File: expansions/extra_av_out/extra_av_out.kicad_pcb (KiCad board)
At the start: 4 copper layers, 75.8 x 88.1 mm, 40 parts, among them J1 Conn_02x25_Odd_Even, J2 SJ1-3533NG, J3 PLT133/T10W, J4 VGA, U1 ADV7125KSTZ140, U2 PCM5142PW, U3 74HCT2G17GW

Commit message: update extra_av_out board to v1.1
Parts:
- removed C12, C14, C6: 10u, custom_components:SM0603_Capa_libcms
- added D2: PESD5V0V4UW, Package_TO_SOT_SMD:SOT-665, B.Cu at (68.4, 78.3)
- added D3: PESD12VL2BT, Package_TO_SOT_SMD:SOT-23, B.Cu at (100.6, 71.0)
- added D4: PESD5V0U4BW, Package_TO_SOT_SMD:SOT-665, B.Cu at (74.7, 70.8)
- added FB1: MPZ1608S102ATA00, custom_components:SM0603_Resistor_libcms, F.Cu at (53.3, 81.9)
- added FB2: MPZ1608S102ATA00, custom_components:SM0603_Resistor_libcms, F.Cu at (53.3, 80.2)
- added MH1: MountingHole, MountingHole:MountingHole_3.2mm_M3_ISO14580, F.Cu at (53.3, 29.0)
- added MH2: MountingHole, MountingHole:MountingHole_3.2mm_M3_ISO14580, F.Cu at (53.3, 86.5)
- added MH3: MountingHole, MountingHole:MountingHole_3.2mm_M3_ISO14580, F.Cu at (115.5, 68.3)
- added MH4: MountingHole, MountingHole:MountingHole_3.2mm_M3_ISO14580_Pad, F.Cu at (94.9, 79.9)
- added MH5: MountingHole, MountingHole:MountingHole_3.2mm_M3_ISO14580_Pad, F.Cu at (66.0, 38.4)
- added Q1: BC847, Package_TO_SOT_SMD:SOT-23, B.Cu at (61.6, 71.8)
- added R10: 47, custom_components:SM0603_Resistor_libcms, B.Cu at (70.3, 70.5)
- added R11: 47, custom_components:SM0603_Resistor_libcms, B.Cu at (72.0, 70.5)
- added R12: 10k, custom_components:SM0603_Resistor_libcms, B.Cu at (58.0, 71.9)
- added R13: 4.7k, custom_components:SM0603_Resistor_libcms, B.Cu at (58.0, 73.6)
- added R9: 47, custom_components:SM0603_Resistor_libcms, B.Cu at (68.6, 70.5)
- moved C9 8.91 mm to (91.9, 68.8), turned to 0 degrees
- moved C5 8.18 mm to (85.6, 70.5)
- moved C8 7.95 mm to (91.9, 65.5), turned to 180 degrees
- moved U2 7.56 mm to (88.7, 65.8)
- moved R1 7.56 mm to (82.1, 68.7)
- moved C3 6.70 mm to (91.9, 70.5), turned to 180 degrees
- moved C7 6.54 mm to (91.9, 67.2), turned to 180 degrees
- moved C10 5.57 mm to (85.6, 68.9), turned to 0 degrees
- moved C4 4.48 mm to (91.9, 63.8), turned to 180 degrees
- moved J2 4.24 mm to (102.6, 82.2)
- moved C13 3.00 mm to (103.5, 68.1)
- moved C21 3.00 mm to (113.5, 73.7)
- moved J3 2.76 mm to (115.0, 76.3)
- moved R2 2.18 mm to (98.8, 67.6)
- moved R3 2.18 mm to (101.0, 67.6)
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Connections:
- net Net-(C11-Pad2) renamed /AL_OUT
- net Net-(C13-Pad1) renamed /AR_OUT
- net Net-(J4-Pad1) renamed /R_OUT
- net Net-(J4-Pad2) renamed /G_OUT
- net Net-(J4-Pad3) renamed /B_OUT
- J1 pad 1: Net-(J1-Pad1) -> unconnected-(J1-Pin_1-Pad1)
- J1 pad 2: Net-(J1-Pad2) -> unconnected-(J1-Pin_2-Pad2)
- J1 pad 3: Net-(J1-Pad3) -> unconnected-(J1-Pin_3-Pad3)
- J1 pad 39: Net-(J1-Pad39) -> unconnected-(J1-Pin_39-Pad39)
- J1 pad 4: Net-(J1-Pad4) -> unconnected-(J1-Pin_4-Pad4)
- J1 pad 41: Net-(J1-Pad41) -> unconnected-(J1-Pin_41-Pad41)
- J1 pad 44: Net-(J1-Pad44) -> unconnected-(J1-Pin_44-Pad44)
- J1 pad 5: Net-(J1-Pad5) -> unconnected-(J1-Pin_5-Pad5)
- J1 pad 6: Net-(J1-Pad6) -> unconnected-(J1-Pin_6-Pad6)
- J4 pad 11: Net-(J4-Pad11) -> unconnected-(J4-ID0/RES-Pad11)
- J4 pad 12: Net-(J4-Pad12) -> unconnected-(J4-ID1/SDA-Pad12)
- J4 pad 15: Net-(J4-Pad15) -> unconnected-(J4-ID3/SCL-Pad15)
- J4 pad 4: Net-(J4-Pad4) -> /VGA_CS_75
- U2 pad 11: /SDA -> /SDA_F
- U2 pad 12: /SCL -> /SCL_F
- U2 pad 13: Net-(U2-Pad13) -> unconnected-(U2-GPIO5/ATT0-Pad13)
- U2 pad 14: Net-(U2-Pad14) -> unconnected-(U2-GPIO4/MAST-Pad14)
- U2 pad 15: Net-(U2-Pad15) -> unconnected-(U2-GPIO3/AGNS-Pad15)
- U2 pad 19: Net-(U2-Pad19) -> unconnected-(U2-GPIO6/FLT-Pad19)
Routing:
- net /SCL_F: track 0.00 -> 61.4 mm, vias 0 -> 2
- net /SCL: track 72.9 -> 13.3 mm, vias 1 -> 0
- net /SDA: track 70.4 -> 11.8 mm, vias 1 -> 0
- net /SDA_F: track 0.00 -> 56.2 mm, vias 0 -> 2
- net /I2S_WS: track 87.4 -> 55.9 mm
- net /I2S_BCK: track 80.7 -> 51.1 mm
- net /I2S_DATA: track 80.5 -> 50.9 mm
- net GND: track 76.1 -> 104.4 mm, vias 440 -> 148
- net /VGA_VS_TTL: track 17.3 -> 25.5 mm
- net Net-(Q1-E): track 0.00 -> 5.99 mm
- net /DVDD5: track 3.12 -> 9.08 mm
- net /VGA_CS_75: track 0.00 -> 4.91 mm
- net /VGA_HS: track 8.39 -> 13.0 mm, vias 0 -> 1
- net Net-(Q1-B): track 0.00 -> 4.09 mm
- net /R_OUT: track 25.2 -> 29.0 mm, vias 0 -> 1
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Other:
- board size 75.8 x 88.1 mm -> 76.3 x 88.1 mm
- net class Default removed
- board text added: "extra_av_out v1.1"
- board text removed: "extra_av_out v1.0"

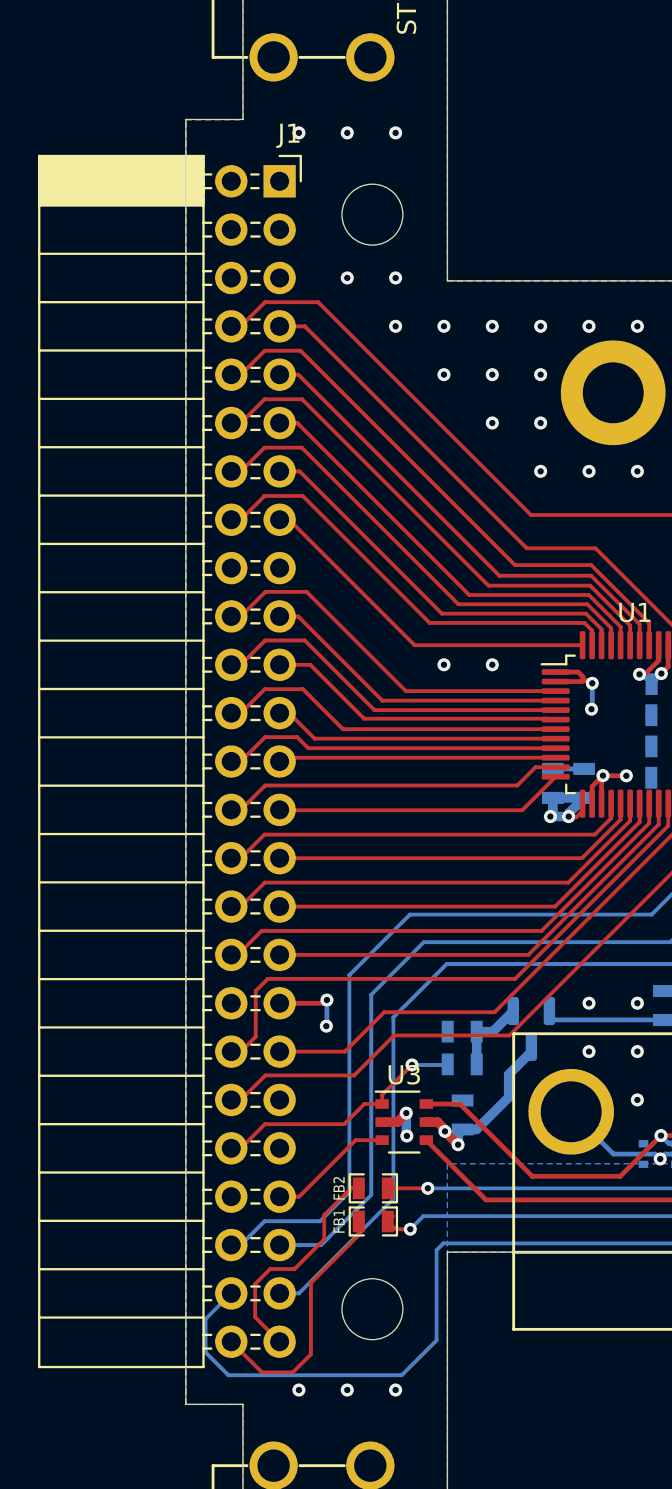
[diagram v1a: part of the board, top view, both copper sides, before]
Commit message: extra_av_out: minor adjustment on J1 position
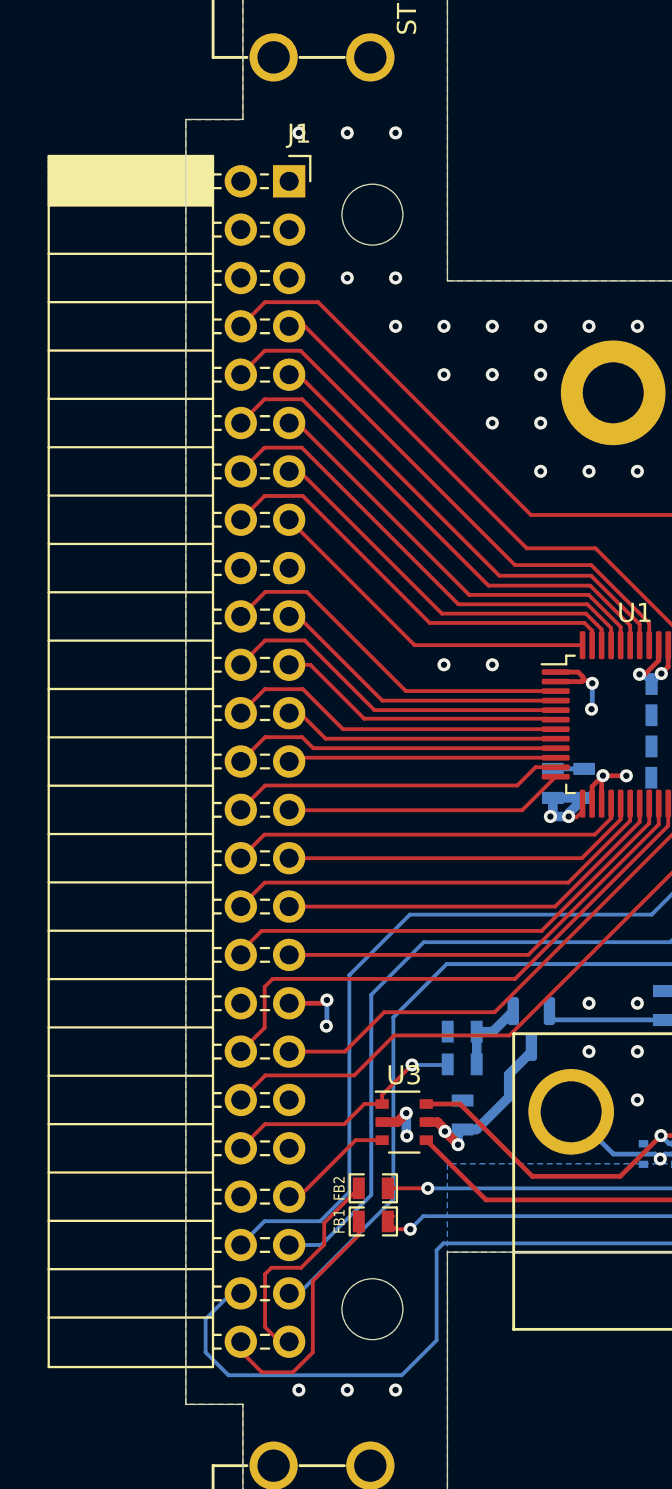
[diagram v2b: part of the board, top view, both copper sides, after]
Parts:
- moved J1 0.50 mm to (48.9, 27.2)
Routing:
- net /SDA: track 11.8 -> 11.3 mm
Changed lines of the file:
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@@
   )
   (footprint "Connector_PinSocket_2.54mm:PinSocket_2x25_P2.54mm_Horizontal" (layer "F.Cu")
-    (at 48.42579 27.24871)
+    (at 48.92579 27.24871)
     (descr "Through hole angled socket strip, 2x25, 2.54mm pitch, 8.51mm socket length, double cols (from Kicad 4.0.7), script generated")
     (tags "Through hole angled socket strip THT 2x25 2.54mm double row")
@@
   (segment (start 57.8 77.86) (end 57.8 77.302) (width 0.5) (layer "B.Cu") (net 11))
   (segment (start 58.04 77.062) (end 58.768 77.062) (width 0.5) (layer "B.Cu") (net 11))
+  (segment (start 47.49708 89.82) (end 49.12 89.82) (width 0.2) (layer "F.Cu") (net 12))
+  (segment (start 50.17 88.77) (end 50.17 85.02) (width 0.2) (layer "F.Cu") (net 12))
+  (segment (start 50.17 85.02) (end 52.586 82.604) (width 0.2) (layer "F.Cu") (net 12))
   (segment (start 52.586 82.604) (end 52.586 81.89) (width 0.2) (layer "F.Cu") (net 12))
   (segment (start 45.88579 88.20871) (end 47.49708 89.82) (width 0.2) (layer "F.Cu") (net 12))
-  (segment (start 49.12 89.82) (end 50.07 88.87) (width 0.2) (layer "F.Cu") (net 12))
-  (segment (start 50.07 88.87) (end 50.07 85.12) (width 0.2) (layer "F.Cu") (net 12))
-  (segment (start 50.07 85.12) (end 52.586 82.604) (width 0.2) (layer "F.Cu") (net 12))
-  (segment (start 47.49708 89.82) (end 49.12 89.82) (width 0.2) (layer "F.Cu") (net 12))
-  (segment (start 50.77 82.83) (end 50.77 81.56) (width 0.2) (layer "F.Cu") (net 13))
-  (segment (start 52.18 80.15) (end 52.586 80.15) (width 0.2) (layer "F.Cu") (net 13))
-  (segment (start 50.77 81.56) (end 52.18 80.15) (width 0.2) (layer "F.Cu") (net 13))
-  (segment (start 49.21 84.39) (end 50.77 82.83) (width 0.2) (layer "F.Cu") (net 13))
-  (segment (start 47.14 85.18) (end 47.93 84.39) (width 0.2) (layer "F.Cu") (net 13))
-  (segment (start 48.42579 88.20871) (end 47.14 86.92292) (width 0.2) (layer "F.Cu") (net 13))
-  (segment (start 47.14 86.92292) (end 47.14 85.18) (width 0.2) (layer "F.Cu") (net 13))
-  (segment (start 47.93 84.39) (end 49.21 84.39) (width 0.2) (layer "F.Cu") (net 13))
+  (segment (start 49.12 89.82) (end 50.17 88.77) (width 0.2) (layer "F.Cu") (net 12))
+  (segment (start 49.55629 84.32371) (end 50.77 83.11) (width 0.2) (layer "F.Cu") (net 13))
+  (segment (start 50.77 83.11) (end 50.77 81.966) (width 0.2) (layer "F.Cu") (net 13))
+  (segment (start 47.66 87.44292) (end 47.66 84.66) (width 0.2) (layer "F.Cu") (net 13))
+  (segment (start 47.66 84.66) (end 47.99629 84.32371) (width 0.2) (layer "F.Cu") (net 13))
+  (segment (start 47.99629 84.32371) (end 49.55629 84.32371) (width 0.2) (layer "F.Cu") (net 13))
+  (segment (start 50.77 81.966) (end 52.586 80.15) (width 0.2) (layer "F.Cu") (net 13))
+  (segment (start 48.42579 88.20871) (end 47.66 87.44292) (width 0.2) (layer "F.Cu") (net 13))
   (segment (start 56.67 83.4) (end 57.03 83.04) (width 0.2) (layer "B.Cu") (net 14))
   (segment (start 110.29 72.36) (end 116.04 72.36) (width 0.2) (layer "B.Cu") (net 14))
@@
   (segment (start 51.85129 72.96871) (end 48.92579 72.96871) (width 0.2) (layer "F.Cu") (net 22))
   (segment (start 53.92 70.9) (end 51.85129 72.96871) (width 0.2) (layer "F.Cu") (net 22))
+  (segment (start 47.64 71.7145) (end 46.38579 72.96871) (width 0.2) (layer "F.Cu") (net 23))
+  (segment (start 60.794538 69.15) (end 48.06 69.15) (width 0.2) (layer "F.Cu") (net 23))
+  (segment (start 48.06 69.15) (end 47.64 69.57) (width 0.2) (layer "F.Cu") (net 23))
   (segment (start 68.84 61.104538) (end 60.794538 69.15) (width 0.2) (layer "F.Cu") (net 23))
+  (segment (start 47.64 69.57) (end 47.64 71.7145) (width 0.2) (layer "F.Cu") (net 23))
   (segment (start 68.84 59.9425) (end 68.84 61.104538) (width 0.2) (layer "F.Cu") (net 23))
-  (segment (start 47.17 69.78) (end 47.17 72.1845) (width 0.2) (layer "F.Cu") (net 23))
-  (segment (start 47.8 69.15) (end 47.17 69.78) (width 0.2) (layer "F.Cu") (net 23))
-  (segment (start 60.794538 69.15) (end 47.8 69.15) (width 0.2) (layer "F.Cu") (net 23))
-  (segment (start 47.17 72.1845) (end 46.38579 72.96871) (width 0.2) (layer "F.Cu") (net 23))
   (segment (start 61.490129 67.88871) (end 48.92579 67.88871) (width 0.2) (layer "F.Cu") (net 24))
   (segment (start 68.34 61.038839) (end 61.490129 67.88871) (width 0.2) (layer "F.Cu") (net 24))
@@
   (segment (start 49.1245 57.53) (end 48.92579 57.72871) (width 0.2) (layer "F.Cu") (net 32))
   (segment (start 62.9275 57.53) (end 49.1245 57.53) (width 0.2) (layer "F.Cu") (net 32))
-  (segment (start 49.349082 56.45) (end 47.6645 56.45) (width 0.2) (layer "F.Cu") (net 33))
-  (segment (start 49.929082 57.03) (end 49.349082 56.45) (width 0.2) (layer "F.Cu") (net 33))
+  (segment (start 49.61 56.45) (end 47.6645 56.45) (width 0.2) (layer "F.Cu") (net 33))
+  (segment (start 50.19 57.03) (end 49.61 56.45) (width 0.2) (layer "F.Cu") (net 33))
   (segment (start 47.6645 56.45) (end 46.38579 57.72871) (width 0.2) (layer "F.Cu") (net 33))
-  (segment (start 62.9275 57.03) (end 49.929082 57.03) (width 0.2) (layer "F.Cu") (net 33))
-  (segment (start 62.9275 56.53) (end 50.26708 56.53) (width 0.2) (layer "F.Cu") (net 34))
-  (segment (start 50.26708 56.53) (end 48.92579 55.18871) (width 0.2) (layer "F.Cu") (net 34))
+  (segment (start 62.9275 57.03) (end 50.19 57.03) (width 0.2) (layer "F.Cu") (net 33))
+  (segment (start 62.9275 56.53) (end 50.84 56.53) (width 0.2) (layer "F.Cu") (net 34))
+  (segment (start 49.49871 55.18871) (end 48.92579 55.18871) (width 0.2) (layer "F.Cu") (net 34))
+  (segment (start 50.84 56.53) (end 49.49871 55.18871) (width 0.2) (layer "F.Cu") (net 34))
   (segment (start 47.6445 53.93) (end 46.38579 55.18871) (width 0.2) (layer "F.Cu") (net 35))
   (segment (start 51.75 56.03) (end 49.65 53.93) (width 0.2) (layer "F.Cu") (net 35))
